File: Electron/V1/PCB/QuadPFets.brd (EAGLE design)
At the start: 99 x 40 mm, 53 parts, among them Q1 BC817-40SMD, Q2 BC817-40SMD, Q3 BC817-40SMD, Q4 BC817-40SMD, U1 MOSFET-PCHANNEL-SOIC8SOIC8, U2 MOSFET-PCHANNEL-SOIC8SOIC8, U3 MOSFET-PCHANNEL-SOIC8SOIC8, U4 MOSFET-PCHANNEL-SOIC8SOIC8, U5 ELECTRONDUALNAMED

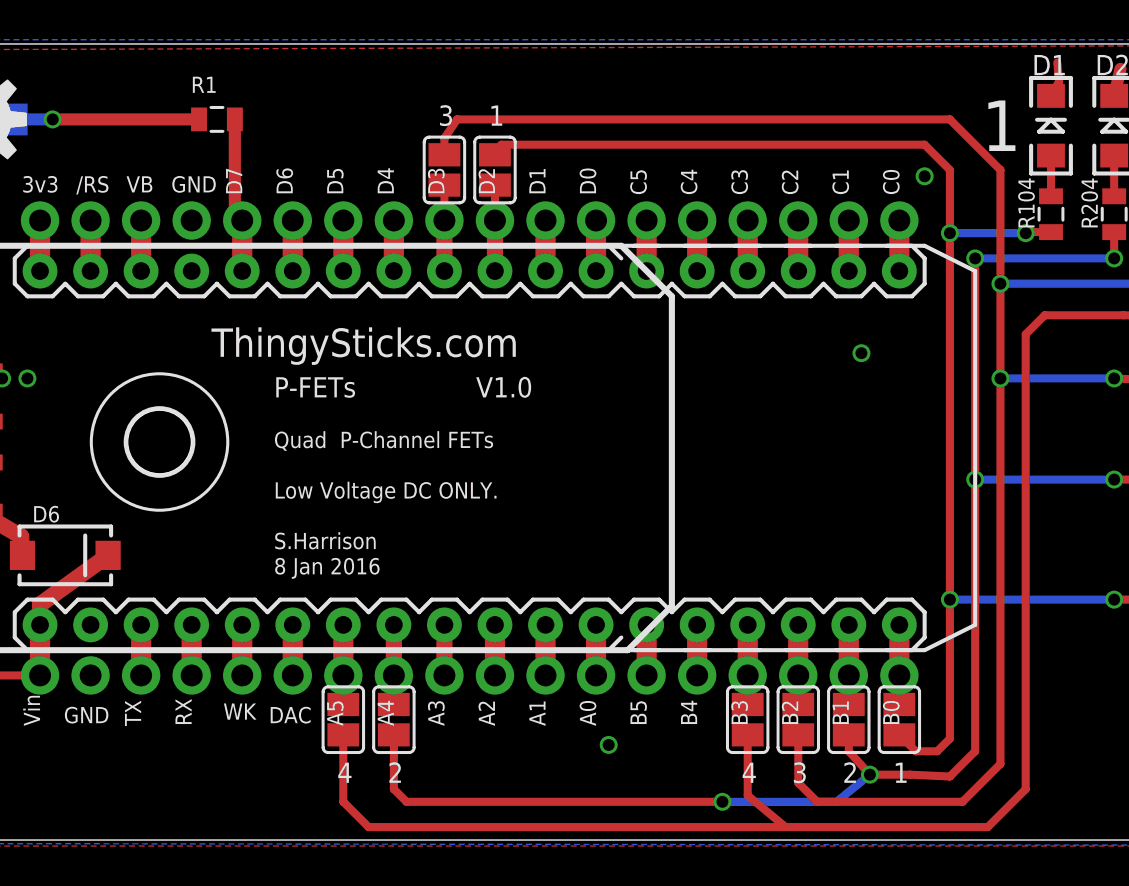
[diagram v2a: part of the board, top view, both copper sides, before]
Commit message: Added more jumper options for PWM source (D0/D1 and TX/RX).
V1.0 order updated at DirtyPCBs
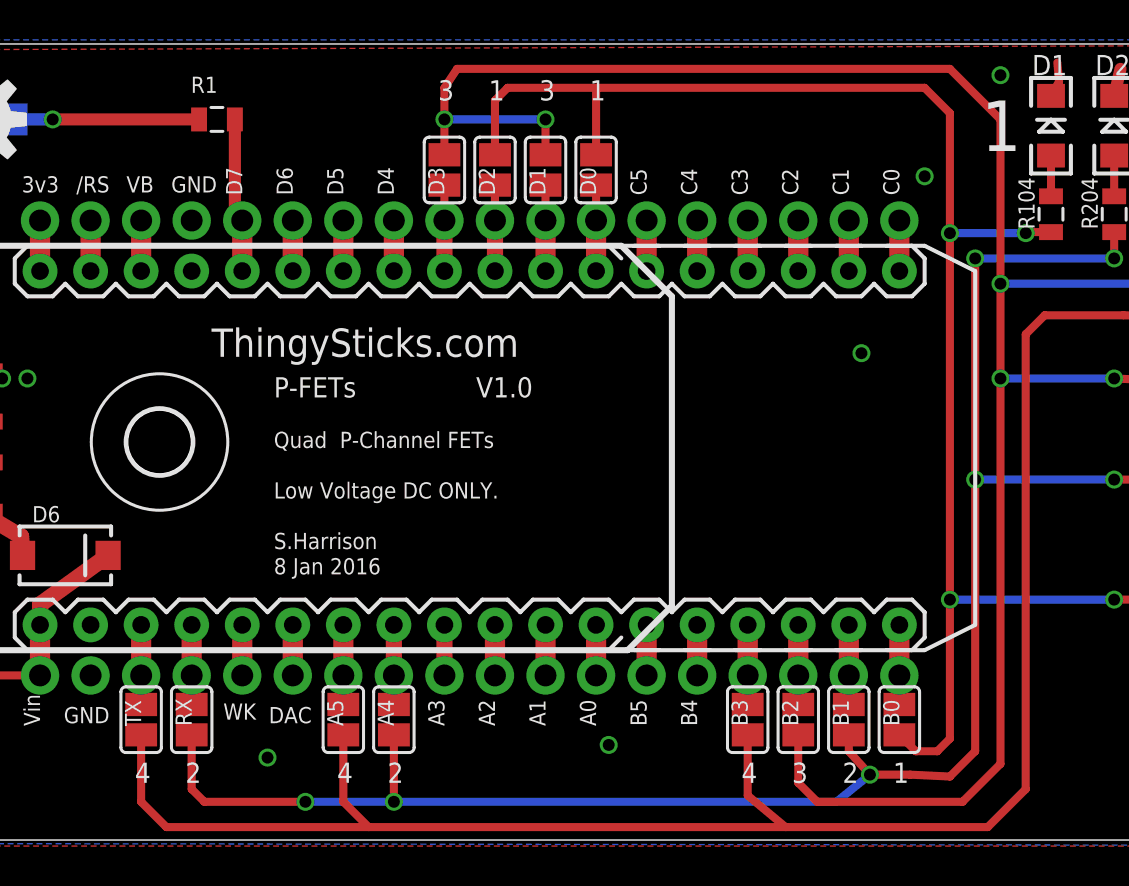
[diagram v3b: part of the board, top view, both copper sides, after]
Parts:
- added SJ10, SJ11, SJ12, SJ7: (no value), jumper:SJ
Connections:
- net CHANNEL_1: now also SJ11.2
- net CHANNEL_2: now also SJ10.1
- net CHANNEL_3: now also SJ12.2
- net CHANNEL_4: now also SJ7.1
- net N$47: now also SJ10.2
- net N$48: now also SJ7.2
- net SCL: now also SJ12.1
- net SDA: now also SJ11.1
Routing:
- net CHANNEL_4: track 82.9 -> 98.2 mm
- net CHANNEL_2: track 77.6 -> 91.2 mm, vias 6 -> 7
- net CHANNEL_3: track 93.1 -> 105.0 mm, vias 4 -> 6
- net CHANNEL_1: track 70.7 -> 79.7 mm
- net SDA: track 2.54 -> 4.32 mm
- net SCL: track 2.54 -> 4.32 mm
- net N$48: track 2.54 -> 4.00 mm
- net N$47: track 2.54 -> 4.00 mm
- net GND: vias 10 -> 12
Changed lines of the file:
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@@
 <text x="58.7375" y="-4.1275" size="1.016" layer="25" font="vector">4</text>
 <text x="61.2775" y="-4.1275" size="1.016" layer="25" font="vector">3</text>
-<text x="43.4975" y="28.8925" size="1.016" layer="25" font="vector">3</text>
+<text x="43.4975" y="30.1625" size="1.016" layer="25" font="vector">3</text>
 <text x="63.8175" y="-4.1275" size="1.016" layer="25" font="vector">2</text>
 <text x="40.9575" y="-4.1275" size="1.016" layer="25" font="vector">2</text>
 <text x="66.3575" y="-4.1275" size="1.016" layer="25" font="vector">1</text>
-<text x="46.0375" y="28.8925" size="1.016" layer="25" font="vector">1</text>
+<text x="46.0375" y="30.1625" size="1.016" layer="25" font="vector">1</text>
 <wire x1="-1.5" y1="13" x2="128.25" y2="13" width="0" layer="48"/>
 <text x="112.0775" y="-3.4925" size="1.778" layer="25" font="vector" rot="R180">GND</text>
@@
 <dimension x1="90" y1="29" x2="90.17" y2="33.02" x3="116.84" y3="31.01" textsize="1.27" layer="47" dtype="vertical"/>
 <dimension x1="90" y1="-3" x2="90.17" y2="-6.985" x3="118.11" y3="-4.9925" textsize="1.27" layer="47" dtype="vertical"/>
+<text x="30.7975" y="-4.1275" size="1.016" layer="25" font="vector">2</text>
+<text x="28.2575" y="-4.1275" size="1.016" layer="25" font="vector">4</text>
+<text x="51.1175" y="30.1625" size="1.016" layer="25" font="vector">1</text>
+<text x="48.5775" y="30.1625" size="1.016" layer="25" font="vector">3</text>
 </plain>
 <attributes>
@@
 <attribute name="VALUE" x="38.735" y="-0.5524" size="0.02" layer="27" rot="R90"/>
 </element>
+<element name="SJ7" library="jumper" package="SJ" value="" x="28.575" y="-0.9525" smashed="yes" rot="R90">
+<attribute name="VALUE" x="28.575" y="-0.5524" size="0.02" layer="27" rot="R90"/>
+</element>
+<element name="SJ10" library="jumper" package="SJ" value="" x="31.115" y="-0.9525" smashed="yes" rot="R90">
+<attribute name="VALUE" x="31.115" y="-0.5524" size="0.02" layer="27" rot="R90"/>
+</element>
+<element name="SJ11" library="jumper" package="SJ" value="" x="51.435" y="26.67" smashed="yes" rot="R90">
+<attribute name="VALUE" x="51.435" y="27.0701" size="0.02" layer="27" rot="R90"/>
+</element>
+<element name="SJ12" library="jumper" package="SJ" value="" x="48.895" y="26.67" smashed="yes" rot="R90">
+<attribute name="VALUE" x="48.895" y="27.0701" size="0.02" layer="27" rot="R90"/>
+</element>
 </elements>
 <signals>
@@
 <via x="52.07" y="-2.2225" extent="1-16" drill="0.6"/>
 <via x="67.945" y="26.3525" extent="1-16" drill="0.6"/>
+<via x="34.925" y="-2.8575" extent="1-16" drill="0.6"/>
+<via x="71.755" y="31.4325" extent="1-16" drill="0.6"/>
 </signal>
 <signal name="N$2">
@@
 <contactref element="U5" pad="RX"/>
 <wire x1="31.115" y1="1.27" x2="31.115" y2="3.81" width="1.016" layer="1"/>
+<contactref element="SJ10" pad="2"/>
+<wire x1="31.115" y1="-0.1905" x2="31.115" y2="1.27" width="0.4064" layer="1"/>
 </signal>
 <signal name="N$48">
@@
 <contactref element="U5" pad="TX"/>
 <wire x1="28.575" y1="3.81" x2="28.575" y2="1.27" width="1.016" layer="1"/>
+<contactref element="SJ7" pad="2"/>
+<wire x1="28.575" y1="-0.1905" x2="28.575" y2="1.27" width="0.4064" layer="1"/>
 </signal>
 <signal name="N$1">
@@
 <contactref element="U5" pad="D0"/>
 <wire x1="51.435" y1="24.13" x2="51.435" y2="21.59" width="1.016" layer="1"/>
+<contactref element="SJ11" pad="1"/>
+<wire x1="51.435" y1="25.908" x2="51.435" y2="24.13" width="0.4064" layer="1"/>
 </signal>
 <signal name="SCL">
@@
 <contactref element="U5" pad="D1"/>
 <wire x1="48.895" y1="21.59" x2="48.895" y2="24.13" width="1.016" layer="1"/>
+<contactref element="SJ12" pad="1"/>
+<wire x1="48.895" y1="25.908" x2="48.895" y2="24.13" width="0.4064" layer="1"/>
 </signal>
 <signal name="CHANNEL_1">
@@
 <wire x1="69.215" y1="-1.905" x2="69.215" y2="5.08" width="0.4064" layer="1"/>
 <wire x1="69.215" y1="5.08" x2="69.215" y2="23.495" width="0.4064" layer="1"/>
-<wire x1="69.215" y1="23.495" x2="69.215" y2="26.67" width="0.4064" layer="1"/>
-<wire x1="69.215" y1="26.67" x2="67.945" y2="27.94" width="0.4064" layer="1"/>
-<wire x1="67.945" y1="27.94" x2="46.6725" y2="27.94" width="0.4064" layer="1"/>
-<wire x1="46.6725" y1="27.94" x2="46.355" y2="27.432" width="0.4064" layer="1"/>
+<wire x1="69.215" y1="23.495" x2="69.215" y2="29.5275" width="0.4064" layer="1"/>
+<wire x1="69.215" y1="29.5275" x2="67.945" y2="30.7975" width="0.4064" layer="1"/>
+<wire x1="67.945" y1="30.7975" x2="51.435" y2="30.7975" width="0.4064" layer="1"/>
+<wire x1="51.435" y1="30.7975" x2="46.99" y2="30.7975" width="0.4064" layer="1"/>
+<wire x1="46.99" y1="30.7975" x2="46.355" y2="30.1625" width="0.4064" layer="1"/>
+<wire x1="46.355" y1="30.1625" x2="46.355" y2="27.432" width="0.4064" layer="1"/>
 <wire x1="69.215" y1="-1.905" x2="68.58" y2="-2.54" width="0.4064" layer="1"/>
 <wire x1="68.58" y1="-2.54" x2="67.5005" y2="-2.54" width="0.4064" layer="1"/>
@@
 <wire x1="73.025" y1="23.495" x2="69.215" y2="23.495" width="0.4064" layer="16"/>
 <via x="69.215" y="23.495" extent="1-16" drill="0.6"/>
+<contactref element="SJ11" pad="2"/>
+<wire x1="51.435" y1="27.432" x2="51.435" y2="30.7975" width="0.4064" layer="1"/>
 </signal>
 <signal name="CHANNEL_2">
@@
 <wire x1="65.1962875" y1="-3.715715625" x2="64.135" y2="-2.54" width="0.4064" layer="1"/>
 <wire x1="64.135" y1="-2.54" x2="64.135" y2="-1.7145" width="0.4064" layer="1"/>
-<wire x1="41.275" y1="-1.7145" x2="41.275" y2="-4.445" width="0.4064" layer="1"/>
-<wire x1="41.275" y1="-4.445" x2="41.91" y2="-5.08" width="0.4064" layer="1"/>
-<wire x1="41.91" y1="-5.08" x2="57.785" y2="-5.08" width="0.4064" layer="1"/>
-<via x="57.785" y="-5.08" extent="1-16" drill="0.6"/>
-<wire x1="57.785" y1="-5.08" x2="63.514503125" y2="-5.08" width="0.4064" layer="16"/>
+<wire x1="41.275" y1="-1.7145" x2="41.275" y2="-5.08" width="0.4064" layer="1"/>
+<via x="41.275" y="-5.08" extent="1-16" drill="0.6"/>
+<wire x1="41.275" y1="-5.08" x2="63.514503125" y2="-5.08" width="0.4064" layer="16"/>
 <wire x1="63.514503125" y1="-5.08" x2="65.1962875" y2="-3.715715625" width="0.4064" layer="16"/>
 <via x="65.1962875" y="-3.715715625" extent="1-16" drill="0.6"/>
@@
 <via x="70.485" y="22.225" extent="1-16" drill="0.6"/>
 <wire x1="70.485" y1="22.225" x2="70.485" y2="11.1125" width="0.4064" layer="1"/>
+<contactref element="SJ10" pad="1"/>
+<wire x1="31.115" y1="-1.7145" x2="31.115" y2="-4.445" width="0.4064" layer="1"/>
+<wire x1="31.115" y1="-4.445" x2="31.75" y2="-5.08" width="0.4064" layer="1"/>
+<wire x1="31.75" y1="-5.08" x2="36.83" y2="-5.08" width="0.4064" layer="1"/>
+<via x="36.83" y="-5.08" extent="1-16" drill="0.6"/>
+<wire x1="36.83" y1="-5.08" x2="41.275" y2="-5.08" width="0.4064" layer="16"/>
 </signal>
 <signal name="D7">
@@
 <wire x1="40.005" y1="-6.35" x2="38.735" y2="-5.08" width="0.4064" layer="1"/>
 <wire x1="38.735" y1="-5.08" x2="38.735" y2="-1.7145" width="0.4064" layer="1"/>
+<contactref element="SJ7" pad="1"/>
+<wire x1="28.575" y1="-1.7145" x2="28.575" y2="-5.08" width="0.4064" layer="1"/>
+<wire x1="28.575" y1="-5.08" x2="29.845" y2="-6.35" width="0.4064" layer="1"/>
+<wire x1="29.845" y1="-6.35" x2="40.005" y2="-6.35" width="0.4064" layer="1"/>
 </signal>
 <signal name="CHANNEL_3">
@@
 <wire x1="62.5475" y1="-5.08" x2="61.595" y2="-4.1275" width="0.4064" layer="1"/>
 <wire x1="61.595" y1="-4.1275" x2="61.595" y2="-1.7145" width="0.4064" layer="1"/>
-<wire x1="43.815" y1="27.432" x2="43.815" y2="28.2575" width="0.4064" layer="1"/>
-<wire x1="43.815" y1="28.2575" x2="44.45" y2="29.21" width="0.4064" layer="1"/>
-<wire x1="44.45" y1="29.21" x2="69.215" y2="29.21" width="0.4064" layer="1"/>
-<wire x1="69.215" y1="29.21" x2="71.755" y2="26.67" width="0.4064" layer="1"/>
-<wire x1="71.755" y1="26.67" x2="71.755" y2="20.955" width="0.4064" layer="1"/>
+<wire x1="43.815" y1="27.432" x2="43.815" y2="27.94" width="0.4064" layer="1"/>
+<wire x1="43.815" y1="29.21" x2="43.815" y2="30.7975" width="0.4064" layer="1"/>
+<wire x1="43.815" y1="30.7975" x2="44.45" y2="31.75" width="0.4064" layer="1"/>
+<wire x1="44.45" y1="31.75" x2="69.215" y2="31.75" width="0.4064" layer="1"/>
+<wire x1="69.215" y1="31.75" x2="71.755" y2="29.21" width="0.4064" layer="1"/>
+<wire x1="71.755" y1="29.21" x2="71.755" y2="20.955" width="0.4064" layer="1"/>
 <contactref element="R303" pad="2"/>
 <contactref element="R304" pad="1"/>
@@
 <wire x1="80.645" y1="20.955" x2="71.755" y2="20.955" width="0.4064" layer="16"/>
 <via x="71.755" y="20.955" extent="1-16" drill="0.6"/>
+<contactref element="SJ12" pad="2"/>
+<wire x1="48.895" y1="27.432" x2="48.895" y2="29.21" width="0.4064" layer="1"/>
+<via x="48.895" y="29.21" extent="1-16" drill="0.6"/>
+<wire x1="48.895" y1="29.21" x2="43.815" y2="29.21" width="0.4064" layer="16"/>
+<via x="43.815" y="29.21" extent="1-16" drill="0.6"/>
+<wire x1="43.815" y1="29.21" x2="43.815" y2="27.94" width="0.4064" layer="1"/>
 </signal>
 <signal name="N$30">
